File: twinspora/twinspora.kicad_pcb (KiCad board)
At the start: 4 copper layers, 76.9 x 36.8 mm, 176 parts, among them J1 TYPE-C-31-M-12, J10 XY-SH1_0-4A61, J12 XY-SH1_0-5A61, J13 Conn_01x02, J14 Conn_01x03, J15 Conn_01x03, J2 XT30U-M, J3 XT60PW-M, J4 Conn_01x02, J5 XY-SH1_0-3A61, J6 XY-SH1_0-3A61, J7 Conn_01x02, J8 XY-SH1_0-6A51, J9 XY-SH1_0-6A51, Q1 AO3401A, SW2 TS1187A26020, SW3 TS1187A26020, U1 STM32G473RBTx, U10 SRV05-4A, U11 SRV05-4A, U12 SRV05-4A, U2 SRV05-4A, U3 SRV05-4A, U4 XC6206P332MR, U5 CA-IF1044VD-Q1, U6 DRV8316CRRGFR, U7 DRV8316CRRGFR, U8 MT6701QT, U9 MT6701QT, X1 X322512MSB4SI

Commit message: sum stitching vias
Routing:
- net GND: vias 304 -> 311
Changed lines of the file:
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@@
 	)
 	(via
+		(at 79.064 125.014)
+		(size 0.45)
+		(drill 0.3)
+		(layers "F.Cu" "B.Cu")
+		(free yes)
+		(net "GND")
+	)
+	(via
 		(at 86.1 122.3)
 		(size 0.45)
@@
 	)
 	(via
+		(at 77.286 121.966)
+		(size 0.45)
+		(drill 0.3)
+		(layers "F.Cu" "B.Cu")
+		(free yes)
+		(net "GND")
+	)
+	(via
 		(at 116.25 116.5)
 		(size 0.45)
@@
 	)
 	(via
+		(at 79.064 123.998)
+		(size 0.45)
+		(drill 0.3)
+		(layers "F.Cu" "B.Cu")
+		(free yes)
+		(net "GND")
+	)
+	(via
 		(at 145.25 114.75)
 		(size 0.45)
@@
 	)
 	(via
+		(at 77.409793 117.601262)
+		(size 0.45)
+		(drill 0.3)
+		(layers "F.Cu" "B.Cu")
+		(free yes)
+		(net "GND")
+	)
+	(via
 		(at 115.6 132.6)
 		(size 0.45)
@@
 	)
 	(via
+		(at 78.81 120.95)
+		(size 0.45)
+		(drill 0.3)
+		(layers "F.Cu" "B.Cu")
+		(free yes)
+		(net "GND")
+	)
+	(via
 		(at 129.979752 111.448949)
 		(size 0.45)
@@
 	)
 	(via
+		(at 79.040285 118.863986)
+		(size 0.45)
+		(drill 0.3)
+		(layers "F.Cu" "B.Cu")
+		(free yes)
+		(net "GND")
+	)
+	(via
 		(at 120 116)
 		(size 0.45)
@@
 	)
 	(via
+		(at 77.794 114.092)
+		(size 0.45)
+		(drill 0.3)
+		(layers "F.Cu" "B.Cu")
+		(free yes)
+		(net "GND")
+	)
+	(via
 		(at 82.7 121.2)
 		(size 0.45)
@@
 	)
 	(segment
-		(start 132.15 124.65)
-		(end 132.15 127.73911)
-		(width 0.3)
-		(layer "In2.Cu")
-		(net "+5V")
-	)
-	(segment
-		(start 111.528858 134.3)
-		(end 110.726057 133.497199)
+		(start 125.5 130.5)
+		(end 121.7 134.3)
 		(width 0.8)
 		(layer "In2.Cu")
@@
 	)
 	(segment
-		(start 126.9 130.5)
-		(end 125.5 130.5)
-		(width 0.8)
+		(start 132.15 124.65)
+		(end 132.15 127.73911)
+		(width 0.3)
 		(layer "In2.Cu")
 		(net "+5V")
@@
 	)
 	(segment
-		(start 86.624013 135.5)
-		(end 78.25 127.125987)
+		(start 126.9 130.5)
+		(end 125.5 130.5)
 		(width 0.8)
 		(layer "In2.Cu")
@@
 	)
 	(segment
-		(start 90.544582 133.946)
-		(end 88.990582 135.5)
+		(start 131.5 124)
+		(end 129.406291 126.093709)
 		(width 0.8)
 		(layer "In2.Cu")
@@
 	)
 	(segment
-		(start 110.726057 133.497199)
-		(end 104.486901 133.497199)
-		(width 0.8)
-		(layer "In2.Cu")
-		(net "+5V")
-	)
-	(segment
 		(start 135.60942 129)
 		(end 142.5 129)
@@
 	)
 	(segment
-		(start 121.7 134.3)
-		(end 111.528858 134.3)
+		(start 77.794 126.669987)
+		(end 77.794 123.456)
 		(width 0.8)
 		(layer "In2.Cu")
@@
 	)
 	(segment
-		(start 78.25 127.125987)
-		(end 78.25 123)
+		(start 131.5 124)
+		(end 132.15 124.65)
+		(width 0.3)
+		(layer "In2.Cu")
+		(net "+5V")
+	)
+	(segment
+		(start 90.544582 133.946)
+		(end 88.990582 135.5)
 		(width 0.8)
 		(layer "In2.Cu")
@@
 	)
 	(segment
-		(start 131.5 124)
-		(end 129.406291 126.093709)
+		(start 77.794 123.456)
+		(end 79.75 121.5)
 		(width 0.8)
 		(layer "In2.Cu")
@@
 	)
 	(segment
-		(start 131.5 124)
-		(end 132.15 124.65)
-		(width 0.3)
+		(start 88.990582 135.5)
+		(end 86.624013 135.5)
+		(width 0.8)
 		(layer "In2.Cu")
 		(net "+5V")
 	)
 	(segment
-		(start 104.486901 133.497199)
-		(end 104.0381 133.946)
+		(start 110.726057 133.497199)
+		(end 104.486901 133.497199)
 		(width 0.8)
 		(layer "In2.Cu")
@@
 	)
 	(segment
-		(start 79.75 121.5)
-		(end 79.75 120)
+		(start 121.7 134.3)
+		(end 111.528858 134.3)
 		(width 0.8)
 		(layer "In2.Cu")
@@
 	)
 	(segment
-		(start 78.25 123)
-		(end 79.75 121.5)
+		(start 79.75 121.5)
+		(end 79.75 120)
 		(width 0.8)
 		(layer "In2.Cu")
@@
 	)
 	(segment
-		(start 104.0381 133.946)
-		(end 90.544582 133.946)
+		(start 128.975 127.3)
+		(end 128.975 128.425)
 		(width 0.8)
 		(layer "In2.Cu")
@@
 	)
 	(segment
-		(start 125.5 130.5)
-		(end 121.7 134.3)
+		(start 104.486901 133.497199)
+		(end 104.0381 133.946)
 		(width 0.8)
 		(layer "In2.Cu")
@@
 	)
 	(segment
-		(start 88.990582 135.5)
-		(end 86.624013 135.5)
+		(start 104.0381 133.946)
+		(end 90.544582 133.946)
 		(width 0.8)
 		(layer "In2.Cu")
@@
 	)
 	(segment
-		(start 128.975 128.425)
-		(end 126.9 130.5)
+		(start 86.624013 135.5)
+		(end 77.794 126.669987)
 		(width 0.8)
 		(layer "In2.Cu")
@@
 	)
 	(segment
-		(start 128.975 127.3)
-		(end 128.975 128.425)
+		(start 128.975 128.425)
+		(end 126.9 130.5)
 		(width 0.8)
 		(layer "In2.Cu")
@@
 	)
 	(segment
+		(start 111.528858 134.3)
+		(end 110.726057 133.497199)
+		(width 0.8)
+		(layer "In2.Cu")
+		(net "+5V")
+	)
+	(segment
 		(start 113.4 132.9)
 		(end 113.78337 132.9)
@@
 	)
 	(segment
-		(start 78.449999 118.027502)
-		(end 78.449999 125.835404)
+		(start 78.048 125.433406)
+		(end 82.307297 129.692703)
+		(width 0.5)
+		(layer "F.Cu")
+		(net "VBUS")
+	)
+	(segment
+		(start 78.048 118.429501)
+		(end 78.048 125.433406)
 		(width 0.5)
 		(layer "F.Cu")
@@
 	)
 	(segment
-		(start 79.000001 115.960315)
-		(end 79.000001 117.4775)
+		(start 78.449999 118.027502)
+		(end 78.048 118.429501)
 		(width 0.5)
 		(layer "F.Cu")
@@
 	)
 	(segment
-		(start 78.449999 125.835404)
-		(end 82.307297 129.692703)
+		(start 79.000001 115.960315)
+		(end 79.000001 117.4775)
 		(width 0.5)
 		(layer "F.Cu")

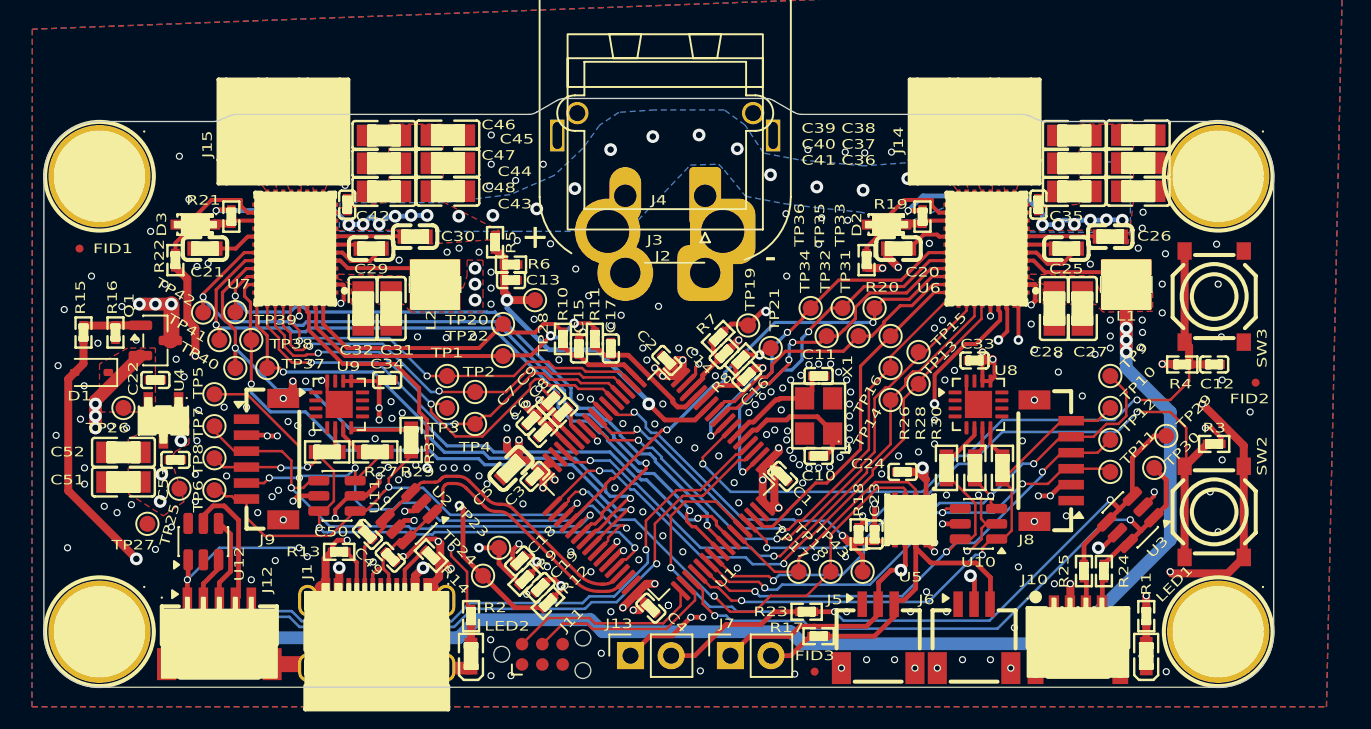
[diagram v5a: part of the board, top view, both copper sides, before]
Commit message: metric hole spacing
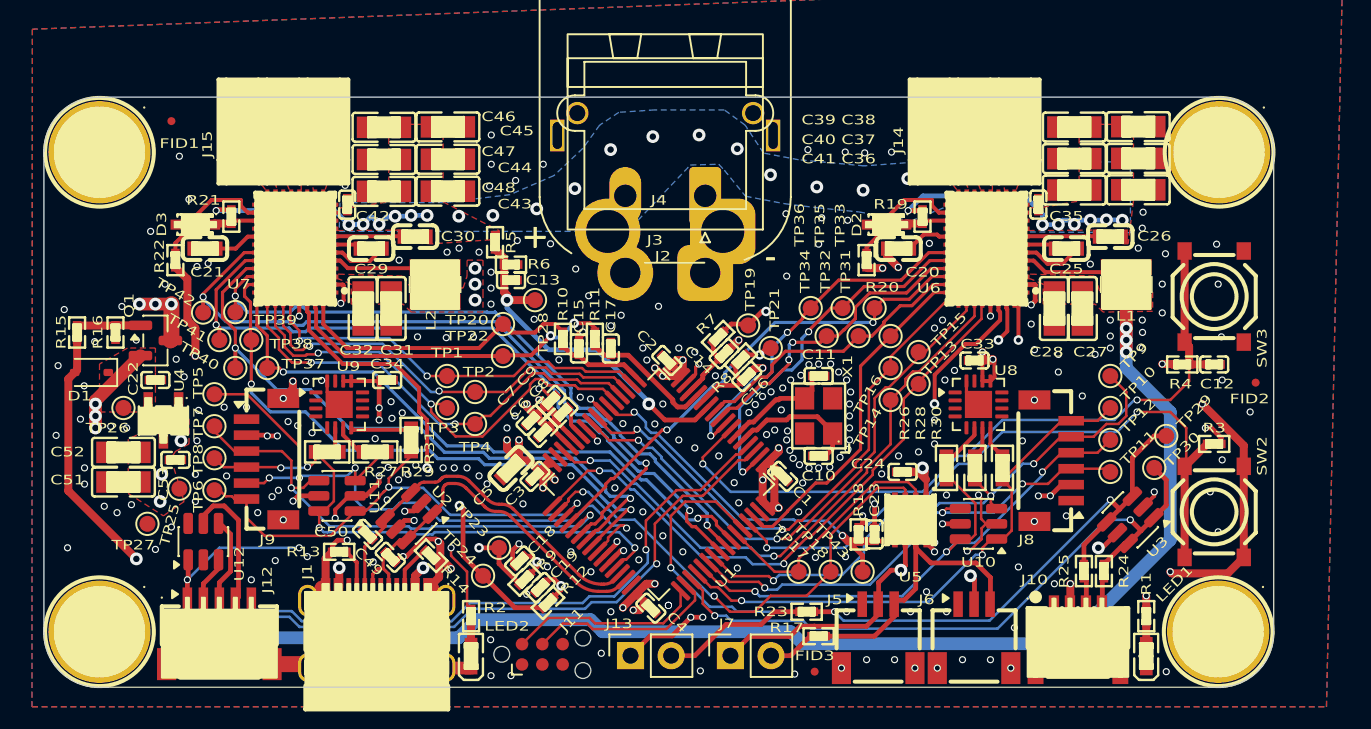
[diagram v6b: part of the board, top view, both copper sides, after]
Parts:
- moved FID1 9.83 mm to (84.5, 102.3)
- moved H16 1.50 mm to (150.1, 104.2)
- moved H4 1.50 mm to (150.1, 104.2)
- moved H1 1.50 mm to (80.0, 104.2)
- moved H13 1.50 mm to (80.0, 104.2)
- moved C38 0.53 mm to (145.0, 102.6)
- moved C39 0.53 mm to (141.0, 102.7)
- moved C46 0.51 mm to (97.8, 102.7)
- moved C45 0.51 mm to (101.8, 102.7)
- moved R15 0.40 mm to (78.6, 115.5)
- moved C37 0.29 mm to (145.0, 104.6)
- moved C40 0.29 mm to (141.0, 104.6)
- moved C44 0.24 mm to (101.8, 104.7)
- moved C47 0.24 mm to (97.8, 104.7)
- moved C36 0.09 mm to (145.0, 106.6)
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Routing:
- net GND: vias 311 -> 310
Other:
- board size 76.9 x 36.8 mm -> 76.9 x 36.9 mm
